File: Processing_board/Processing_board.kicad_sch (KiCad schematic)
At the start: 29 parts, among them J1 Conn_01x08_Pin, J12 Conn_01x02_Pin, J2 Conn_01x08_Pin, J3 Conn_01x06_Pin, J4 Conn_01x03_Pin, J5 Conn_01x03_Pin, J6 Conn_01x02_Pin, SW1 TL3305BF100QG, SW2 TL3305BF100QG, U1 STM32WBA63CIU6

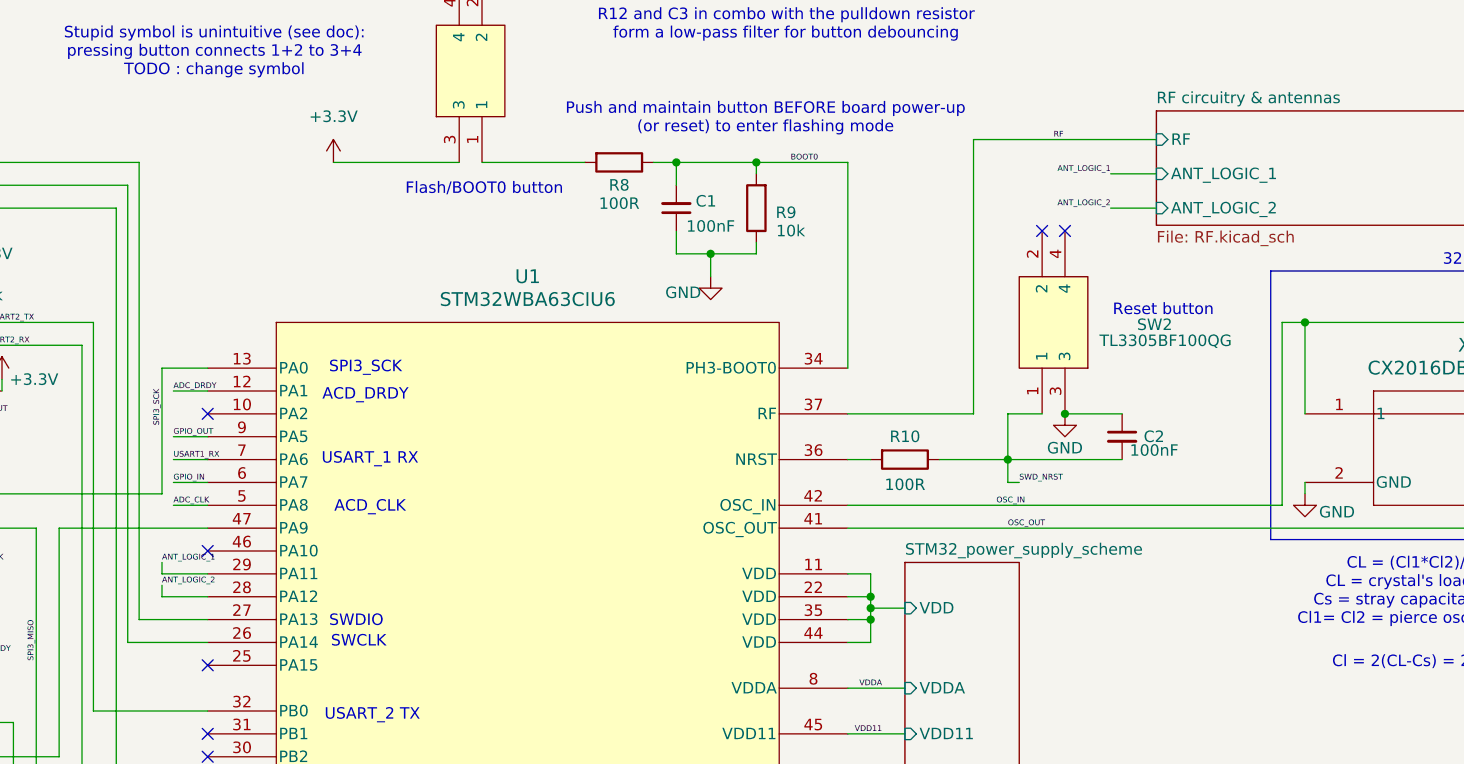
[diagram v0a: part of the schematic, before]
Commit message: RF_circuit schematic updated and board adapted
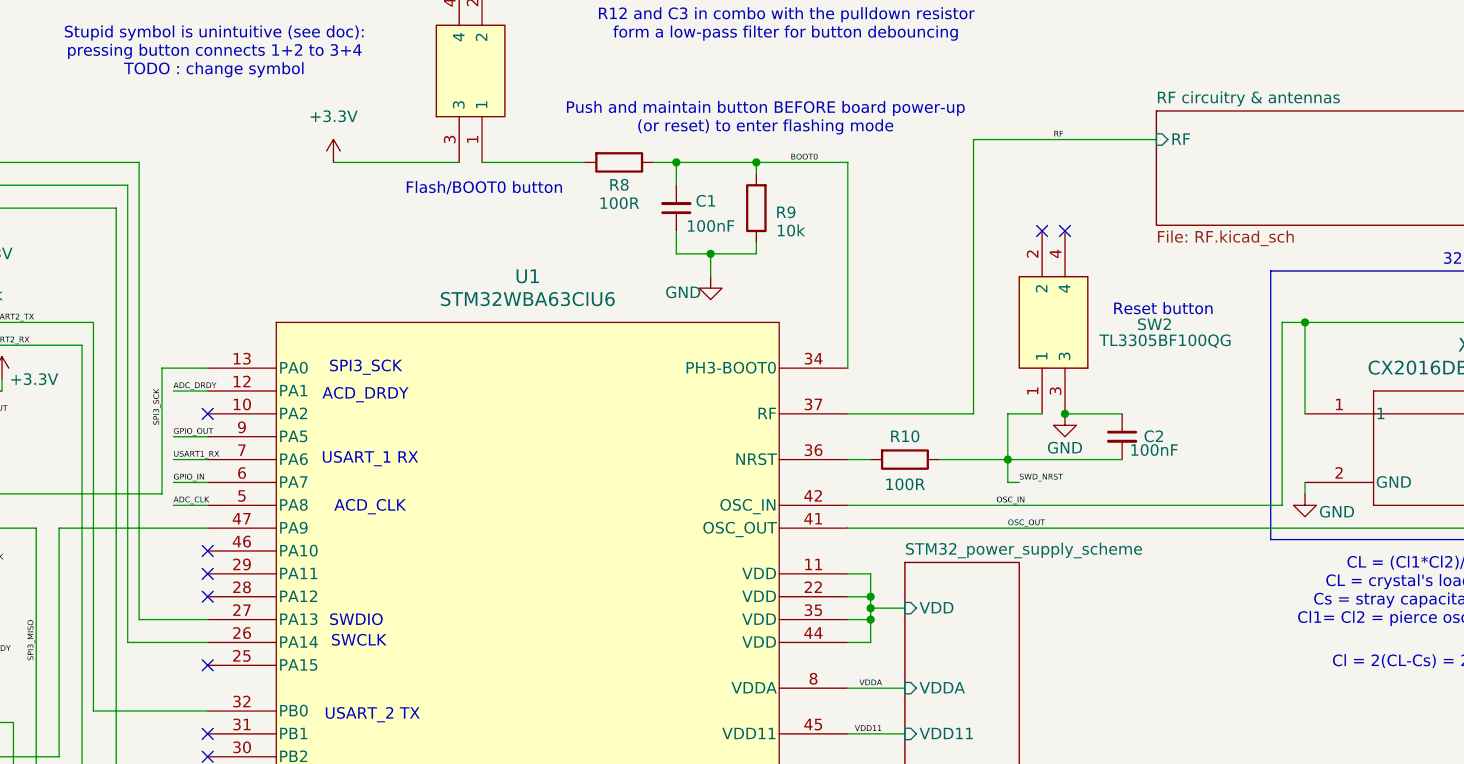
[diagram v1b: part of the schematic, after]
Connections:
- net ANT_LOGIC_1: no longer names the net of U1.29 (PA11)
- net ANT_LOGIC_2: no longer names the net of U1.28 (PA12)
- no-connect marks 13 -> 15
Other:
- sheet RF circuitry & antennas ports: added none; removed ANT_LOGIC_1, ANT_LOGIC_2
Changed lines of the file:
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@@
 	)
 	(no_connect
+		(at 105.41 82.55)
+	)
+	(no_connect
 		(at 105.41 110.49)
 	)
@@
 	)
 	(no_connect
+		(at 105.41 85.09)
+	)
+	(no_connect
 		(at 105.41 102.87)
 	)
@@
 	(wire
 		(pts
-			(xy 100.33 81.28) (xy 100.33 82.55)
-		)
-		(stroke
-			(width 0)
-			(type default)
-		)
-	)
-	(wire
-		(pts
 			(xy 186.69 69.85) (xy 194.31 69.85)
 		)
@@
 	(wire
 		(pts
-			(xy 100.33 83.82) (xy 100.33 85.09)
-		)
-		(stroke
-			(width 0)
-			(type default)
-		)
-	)
-	(wire
-		(pts
 			(xy 176.53 140.97) (xy 182.88 140.97)
 		)
@@
 	(wire
 		(pts
-			(xy 100.33 82.55) (xy 105.41 82.55)
-		)
-		(stroke
-			(width 0)
-			(type default)
-		)
-	)
-	(wire
-		(pts
 			(xy 77.47 62.23) (xy 77.47 64.77)
 		)
@@
 	(wire
 		(pts
-			(xy 205.74 41.91) (xy 210.82 41.91)
-		)
-		(stroke
-			(width 0)
-			(type default)
-		)
-	)
-	(wire
-		(pts
 			(xy 161.29 46.99) (xy 161.29 49.53)
 		)
@@
 	(wire
 		(pts
-			(xy 205.74 38.1) (xy 210.82 38.1)
-		)
-		(stroke
-			(width 0)
-			(type default)
-		)
-	)
-	(wire
-		(pts
 			(xy 100.33 59.69) (xy 105.41 59.69)
 		)
@@
 	(wire
 		(pts
-			(xy 100.33 85.09) (xy 105.41 85.09)
-		)
-		(stroke
-			(width 0)
-			(type default)
-		)
-	)
-	(wire
-		(pts
 			(xy 176.53 69.85) (xy 179.07 69.85)
 		)
@@
 		)
 	)
-	(label "ANT_LOGIC_1"
-		(at 100.33 81.28 0)
-		(effects
-			(font
-				(size 0.635 0.635)
-			)
-			(justify left bottom)
-		)
-	)
 	(label "GPIO_OUT"
 		(at 101.6 67.31 0)
@@
 		)
 	)
-	(label "ANT_LOGIC_2"
-		(at 205.74 41.91 180)
-		(effects
-			(font
-				(size 0.635 0.635)
-			)
-			(justify right bottom)
-		)
-	)
 	(label "USART2_TX"
 		(at 81.0838 54.61 0)
@@
 		)
 	)
-	(label "ANT_LOGIC_1"
-		(at 205.74 38.1 180)
-		(effects
-			(font
-				(size 0.635 0.635)
-			)
-			(justify right bottom)
-		)
-	)
 	(label "LED"
 		(at 97.79 115.57 0)
@@
 		)
 	)
-	(label "ANT_LOGIC_2"
-		(at 100.33 83.82 0)
-		(effects
-			(font
-				(size 0.635 0.635)
-			)
-			(justify left bottom)
-		)
-	)
 	(label "LED"
 		(at 95.25 140.97 0)
@@
 			(effects
 				(font
-					(size 1.27 1.27)
-				)
-				(justify left)
-			)
-		)
-		(pin "ANT_LOGIC_1" input
-			(at 210.82 38.1 180)
-			(effects
-				(font
-					(size 1.27 1.27)
-				)
-				(justify left)
-			)
-		)
-		(pin "ANT_LOGIC_2" input
-			(at 210.82 41.91 180)
-			(effects
-				(font
